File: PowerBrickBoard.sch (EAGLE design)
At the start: 1 part

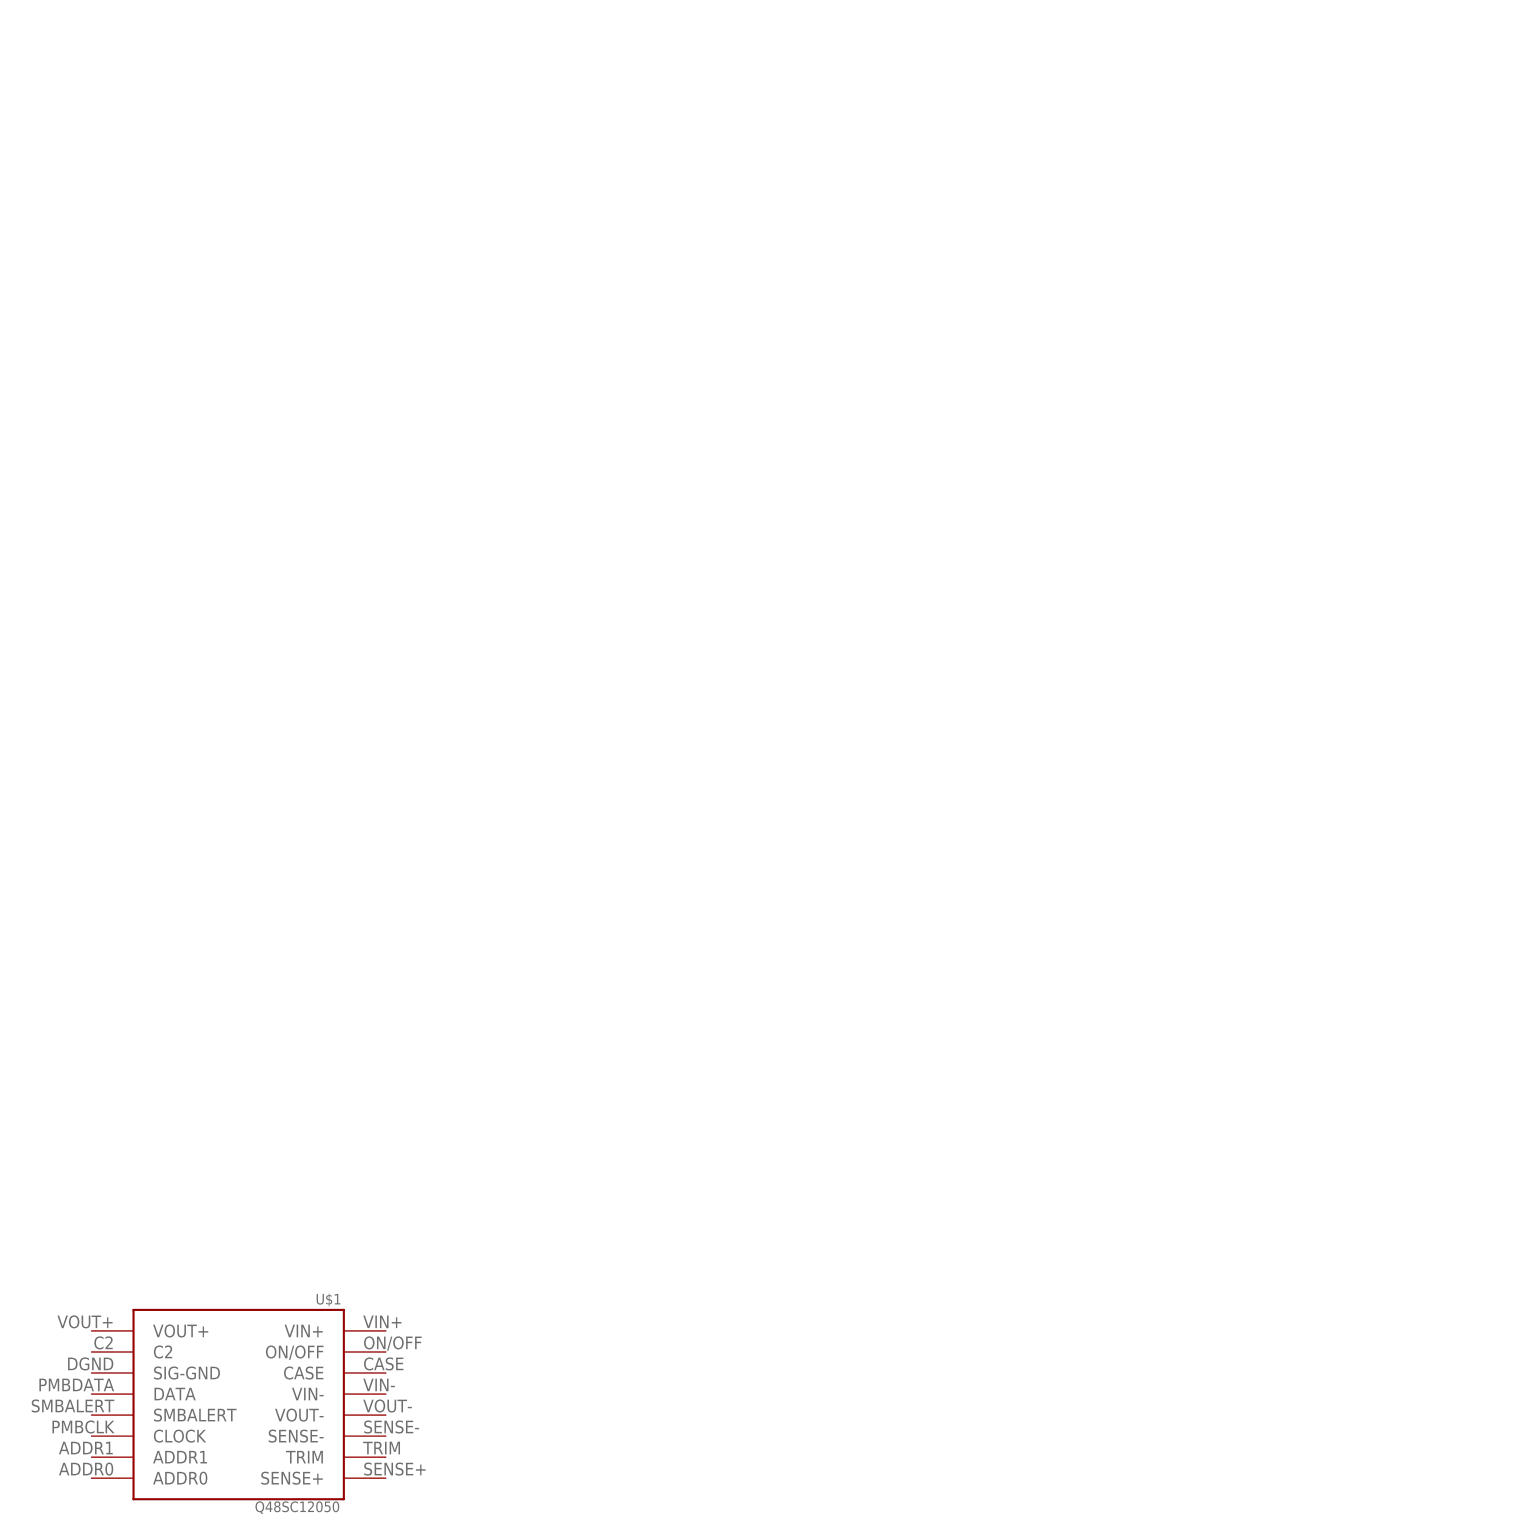
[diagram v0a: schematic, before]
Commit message: added connectors
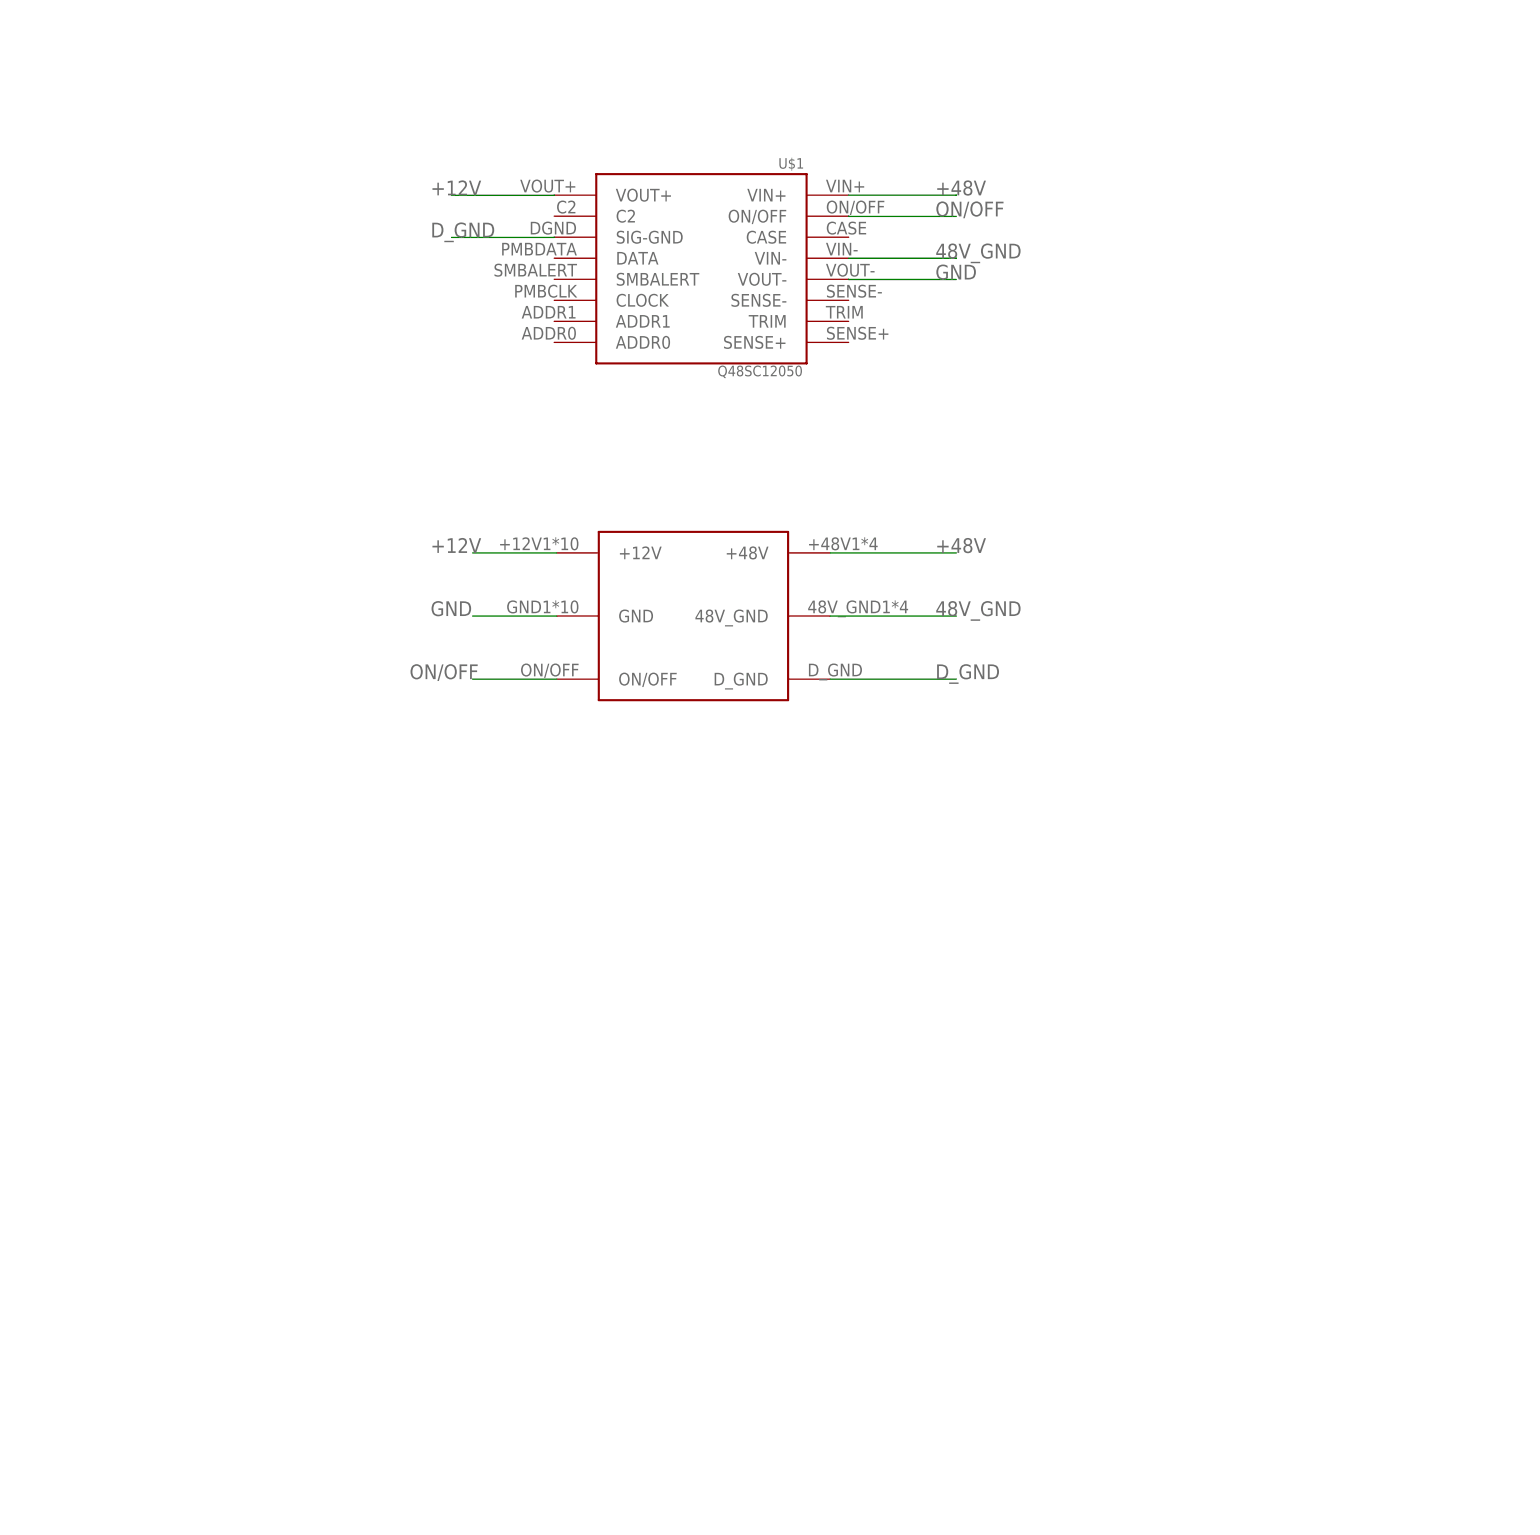
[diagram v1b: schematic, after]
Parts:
- added U$2: BRICK_TO_POWER_DIST_WHOLE, PDB_TO_BRICKS:BRICK_TO_POWER_DIST_WHOLE
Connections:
- new net +12V: U$1.VOUT+, U$2.+12V
- new net +48V: U$1.VIN+, U$2.+48V
- new net 48V_GND: U$1.VIN-, U$2.48V_GND
- new net D_GND: U$1.SIG-GND, U$2.D_GND
- new net GND: U$1.VOUT-, U$2.GND
- new net ON/OFF: U$1.ON/OFF, U$2.ON/OFF
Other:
- moved on the sheet: U$1

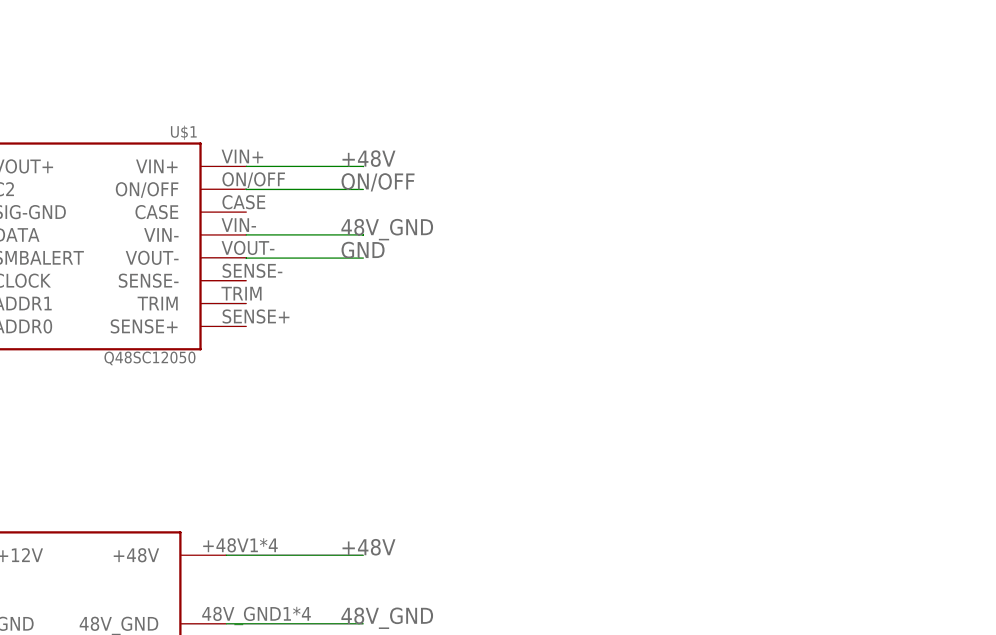
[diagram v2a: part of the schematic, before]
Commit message: Added capacitors
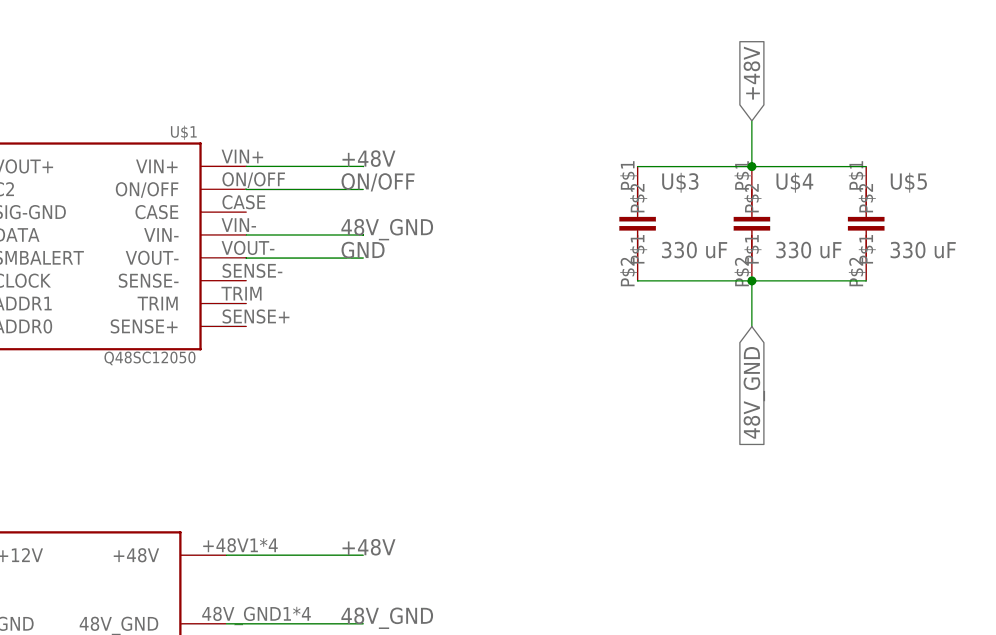
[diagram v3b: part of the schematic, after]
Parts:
- added U$3, U$4, U$5: 330 uF, UCM1H331MNL1GS:UCM1H331MNL1GS
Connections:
- net +48V: now also U$3.P$1, U$4.P$1, U$5.P$1
- net 48V_GND: now also U$3.P$2, U$4.P$2, U$5.P$2
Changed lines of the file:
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@@
 <?xml version="1.0" encoding="utf-8"?>
 <!DOCTYPE eagle SYSTEM "eagle.dtd">
-<eagle version="9.1.3">
+<eagle version="9.2.2">
 <drawing>
 <settings>
@@
 <part name="FRAME1" library="frames" library_urn="urn:adsk.eagle:library:229" deviceset="A4L-LOC" device=""/>
 <part name="U$2" library="PDB_TO_BRICKS" deviceset="BRICK_TO_POWER_DIST_WHOLE" device=""/>
+<part name="U$3" library="UCM1H331MNL1GS" deviceset="UCM1H331MNL1GS" device="" value="330 uF"/>
+<part name="U$4" library="UCM1H331MNL1GS" deviceset="UCM1H331MNL1GS" device="" value="330 uF"/>
+<part name="U$5" library="UCM1H331MNL1GS" deviceset="UCM1H331MNL1GS" device="" value="330 uF"/>
 </parts>
 <sheets>
@@
 </plain>
 <instances>
-<instance part="U$1" gate="G$1" x="55.88" y="137.16" rot="MR0"/>
-<instance part="FRAME1" gate="G$1" x="0" y="0"/>
-<instance part="U$2" gate="G$1" x="43.18" y="86.36"/>
+<instance part="U$1" gate="G$1" x="55.88" y="137.16" smashed="yes" rot="MR0">
+<attribute name="NAME" x="67.9958" y="150.5458" size="1.27" layer="95" rot="MR0"/>
+<attribute name="VALUE" x="67.818" y="125.476" size="1.27" layer="95" rot="MR0"/>
+</instance>
+<instance part="FRAME1" gate="G$1" x="0" y="0" smashed="yes">
+<attribute name="DRAWING_NAME" x="217.17" y="15.24" size="2.54" layer="94"/>
+<attribute name="LAST_DATE_TIME" x="217.17" y="10.16" size="2.286" layer="94"/>
+<attribute name="SHEET" x="230.505" y="5.08" size="2.54" layer="94"/>
+</instance>
+<instance part="U$2" gate="G$1" x="43.18" y="86.36" smashed="yes"/>
+<instance part="U$3" gate="G$1" x="116.84" y="142.24" smashed="yes">
+<attribute name="NAME" x="119.38" y="144.78" size="1.778" layer="95"/>
+<attribute name="VALUE" x="119.38" y="137.16" size="1.778" layer="96"/>
+</instance>
+<instance part="U$4" gate="G$1" x="129.54" y="142.24" smashed="yes">
+<attribute name="NAME" x="132.08" y="144.78" size="1.778" layer="95"/>
+<attribute name="VALUE" x="132.08" y="137.16" size="1.778" layer="96"/>
+</instance>
+<instance part="U$5" gate="G$1" x="142.24" y="142.24" smashed="yes">
+<attribute name="NAME" x="144.78" y="144.78" size="1.778" layer="95"/>
+<attribute name="VALUE" x="144.78" y="137.16" size="1.778" layer="96"/>
+</instance>
 </instances>
 <busses>
@@
 <label x="83.82" y="104.14" size="1.778" layer="95"/>
 </segment>
+<segment>
+<pinref part="U$3" gate="G$1" pin="P$1"/>
+<pinref part="U$4" gate="G$1" pin="P$1"/>
+<wire x1="116.84" y1="147.32" x2="129.54" y2="147.32" width="0.1524" layer="91"/>
+<pinref part="U$5" gate="G$1" pin="P$1"/>
+<wire x1="129.54" y1="147.32" x2="142.24" y2="147.32" width="0.1524" layer="91"/>
+<junction x="129.54" y="147.32"/>
+<wire x1="129.54" y1="147.32" x2="129.54" y2="152.4" width="0.1524" layer="91"/>
+<label x="129.54" y="152.4" size="1.778" layer="95" rot="R90" xref="yes"/>
+</segment>
 </net>
 <net name="ON/OFF" class="0">
@@
 <label x="83.82" y="139.7" size="1.778" layer="95"/>
 </segment>
-</net>
+<segment>
+<pinref part="U$3" gate="G$1" pin="P$2"/>
+<pinref part="U$4" gate="G$1" pin="P$2"/>
+<wire x1="116.84" y1="134.62" x2="129.54" y2="134.62" width="0.1524" layer="91"/>
+<pinref part="U$5" gate="G$1" pin="P$2"/>
+<wire x1="129.54" y1="134.62" x2="142.24" y2="134.62" width="0.1524" layer="91"/>
+<junction x="129.54" y="134.62"/>
+<wire x1="129.54" y1="134.62" x2="129.54" y2="129.54" width="0.1524" layer="91"/>
+<label x="129.54" y="129.54" size="1.778" layer="95" rot="R270" xref="yes"/>
+</segment>
+</net>
